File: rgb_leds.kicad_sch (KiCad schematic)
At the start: 28 parts

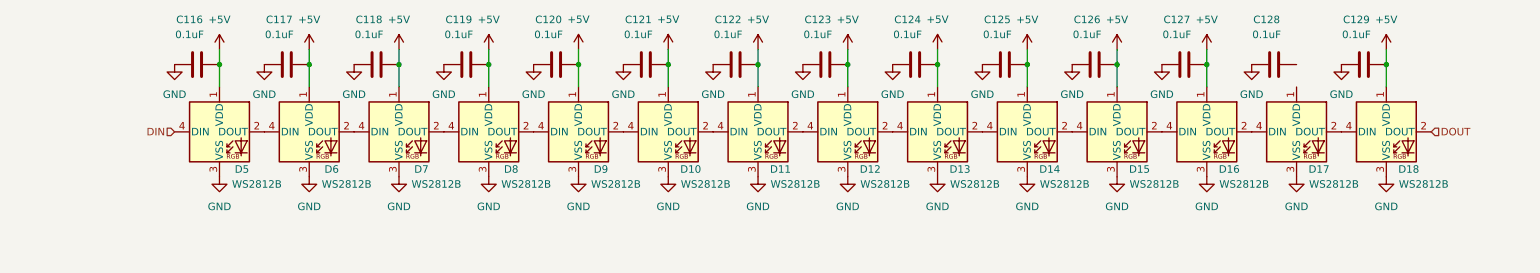
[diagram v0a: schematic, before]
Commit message: usb power source added, need to reassemble to 4-layers
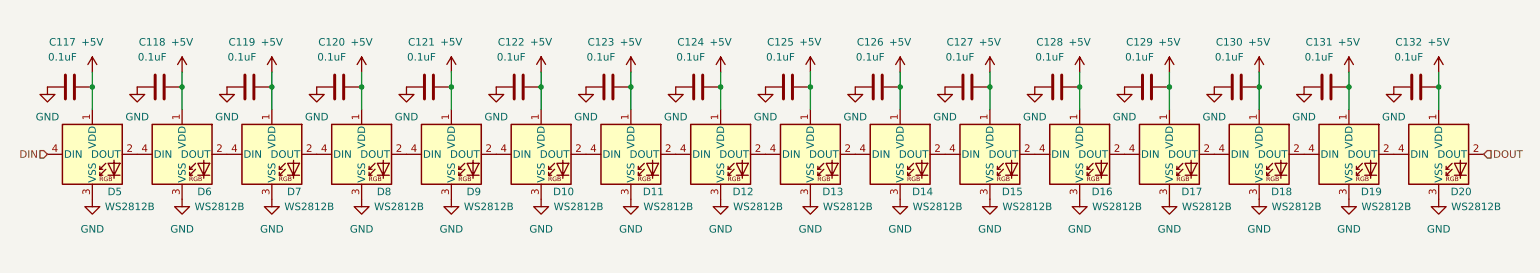
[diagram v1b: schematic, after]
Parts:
- added C129, C130: 0.1uF, Capacitor_SMD:C_0603_1608Metric_Pad1.08x0.95mm_HandSolder, symbol Device:C
- added D17, D18: WS2812B, LED_SMD:LED_WS2812B_PLCC4_5.0x5.0mm_P3.2mm, symbol LED:WS2812B
- renumbered C116 to C117, C117 to C118, C118 to C119, C119 to C120, C120 to C121, C121 to C122, C122 to C123, C123 to C124, C124 to C125, C125 to C126, C126 to C127, C127 to C128, C128 to C131, C129 to C132, D17 to D19, D18 to D20
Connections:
- net +5V: now also C131.2, D19.1 (VDD), C129.2, C130.2, D17.1 (VDD), D18.1 (VDD)
- net GND: now also C129.1, C130.1, D17.3 (VSS), D18.3 (VSS)
- net at D19.4 (DIN): now also D18.2 (DOUT); no longer D16.2 (DOUT)
- new net: D17.2 (DOUT), D18.4 (DIN)
- new net: D16.2 (DOUT), D17.4 (DIN)
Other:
- moved on the sheet: C117, C118, C119, C120, C121, C122, C123, C124, C125, C126, C127, C128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

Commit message: done first iteration of pcb routing, slikscreen still broken
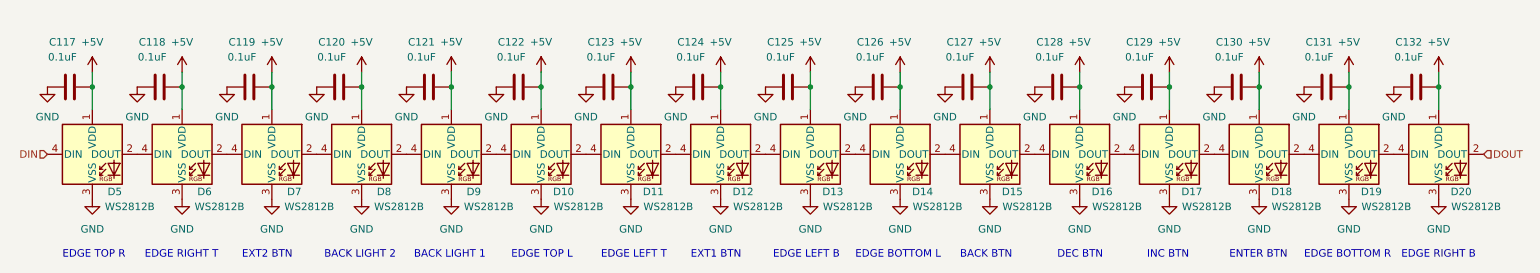
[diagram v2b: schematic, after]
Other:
- note added: "BACK BTN"
- note added: "BACK LIGHT 1"
- note added: "BACK LIGHT 2"
- note added: "DEC BTN"
- note added: "EDGE BOTTOM L"
- note added: "EDGE BOTTOM R"
- note added: "EDGE LEFT B"
- note added: "EDGE LEFT T"
- note added: "EDGE RIGHT B"
- note added: "EDGE RIGHT T"
- note added: "EDGE TOP L"
- note added: "EDGE TOP R"
- note added: "ENTER BTN"
- note added: "EXT1 BTN"
- note added: "EXT2 BTN"
- note added: "INC BTN"

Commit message: mounting holes, fixes silkscreen
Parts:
- renumbered C117 to C115, C118 to C116, C119 to C117, C120 to C118, C121 to C119, C122 to C120, C123 to C121, C124 to C122, C125 to C123, C126 to C124, C127 to C125, C128 to C126, C129 to C127, C130 to C128, C131 to C129, C132 to C130

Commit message: copied own LED footprint, modified silkscreen, minor visual changes in schematics
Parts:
- D10, D11, D12, D13, D14, D15, D16, D17, D18, D19, D20, D5, D6, D7, D8, D9: footprint LED_SMD:LED_WS2812B_PLCC4_5.0x5.0mm_P3.2mm -> airsoft_controller:LED_WS2812B_PLCC4_5.0x5.0mm_P3.2mm
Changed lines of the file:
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@@
     (property "Reference" "D15" (id 0) (at 193.04 97.79 0))
     (property "Value" "WS2812B" (id 1) (at 195.58 100.33 0))
-    (property "Footprint" "LED_SMD:LED_WS2812B_PLCC4_5.0x5.0mm_P3.2mm" (id 2) (at 190.5 99.06 0)
+    (property "Footprint" "airsoft_controller:LED_WS2812B_PLCC4_5.0x5.0mm_P3.2mm" (id 2) (at 190.5 99.06 0)
       (effects (font (size 1.27 1.27)) (justify left top) hide)
     )
@@
     (property "Reference" "D13" (id 0) (at 162.56 97.79 0))
     (property "Value" "WS2812B" (id 1) (at 165.1 100.33 0))
-    (property "Footprint" "LED_SMD:LED_WS2812B_PLCC4_5.0x5.0mm_P3.2mm" (id 2) (at 160.02 99.06 0)
+    (property "Footprint" "airsoft_controller:LED_WS2812B_PLCC4_5.0x5.0mm_P3.2mm" (id 2) (at 160.02 99.06 0)
       (effects (font (size 1.27 1.27)) (justify left top) hide)
     )
@@
     (property "Reference" "D11" (id 0) (at 132.08 97.79 0))
     (property "Value" "WS2812B" (id 1) (at 134.62 100.33 0))
-    (property "Footprint" "LED_SMD:LED_WS2812B_PLCC4_5.0x5.0mm_P3.2mm" (id 2) (at 129.54 99.06 0)
+    (property "Footprint" "airsoft_controller:LED_WS2812B_PLCC4_5.0x5.0mm_P3.2mm" (id 2) (at 129.54 99.06 0)
       (effects (font (size 1.27 1.27)) (justify left top) hide)
     )
@@
     (property "Reference" "D7" (id 0) (at 71.12 97.79 0))
     (property "Value" "WS2812B" (id 1) (at 73.66 100.33 0))
-    (property "Footprint" "LED_SMD:LED_WS2812B_PLCC4_5.0x5.0mm_P3.2mm" (id 2) (at 68.58 99.06 0)
+    (property "Footprint" "airsoft_controller:LED_WS2812B_PLCC4_5.0x5.0mm_P3.2mm" (id 2) (at 68.58 99.06 0)
       (effects (font (size 1.27 1.27)) (justify left top) hide)
     )
@@
     (property "Reference" "D18" (id 0) (at 238.76 97.79 0))
     (property "Value" "WS2812B" (id 1) (at 241.3 100.33 0))
-    (property "Footprint" "LED_SMD:LED_WS2812B_PLCC4_5.0x5.0mm_P3.2mm" (id 2) (at 236.22 99.06 0)
+    (property "Footprint" "airsoft_controller:LED_WS2812B_PLCC4_5.0x5.0mm_P3.2mm" (id 2) (at 236.22 99.06 0)
       (effects (font (size 1.27 1.27)) (justify left top) hide)
     )
@@
     (property "Reference" "D8" (id 0) (at 86.36 97.79 0))
     (property "Value" "WS2812B" (id 1) (at 88.9 100.33 0))
-    (property "Footprint" "LED_SMD:LED_WS2812B_PLCC4_5.0x5.0mm_P3.2mm" (id 2) (at 83.82 99.06 0)
+    (property "Footprint" "airsoft_controller:LED_WS2812B_PLCC4_5.0x5.0mm_P3.2mm" (id 2) (at 83.82 99.06 0)
       (effects (font (size 1.27 1.27)) (justify left top) hide)
     )
@@
     (property "Reference" "D20" (id 0) (at 269.24 97.79 0))
     (property "Value" "WS2812B" (id 1) (at 271.78 100.33 0))
-    (property "Footprint" "LED_SMD:LED_WS2812B_PLCC4_5.0x5.0mm_P3.2mm" (id 2) (at 266.7 99.06 0)
+    (property "Footprint" "airsoft_controller:LED_WS2812B_PLCC4_5.0x5.0mm_P3.2mm" (id 2) (at 266.7 99.06 0)
       (effects (font (size 1.27 1.27)) (justify left top) hide)
     )
@@
     (property "Reference" "D10" (id 0) (at 116.84 97.79 0))
     (property "Value" "WS2812B" (id 1) (at 119.38 100.33 0))
-    (property "Footprint" "LED_SMD:LED_WS2812B_PLCC4_5.0x5.0mm_P3.2mm" (id 2) (at 114.3 99.06 0)
+    (property "Footprint" "airsoft_controller:LED_WS2812B_PLCC4_5.0x5.0mm_P3.2mm" (id 2) (at 114.3 99.06 0)
       (effects (font (size 1.27 1.27)) (justify left top) hide)
     )
@@
     (property "Reference" "D14" (id 0) (at 177.8 97.79 0))
     (property "Value" "WS2812B" (id 1) (at 180.34 100.33 0))
-    (property "Footprint" "LED_SMD:LED_WS2812B_PLCC4_5.0x5.0mm_P3.2mm" (id 2) (at 175.26 99.06 0)
+    (property "Footprint" "airsoft_controller:LED_WS2812B_PLCC4_5.0x5.0mm_P3.2mm" (id 2) (at 175.26 99.06 0)
       (effects (font (size 1.27 1.27)) (justify left top) hide)
     )
@@
     (property "Reference" "D12" (id 0) (at 147.32 97.79 0))
     (property "Value" "WS2812B" (id 1) (at 149.86 100.33 0))
-    (property "Footprint" "LED_SMD:LED_WS2812B_PLCC4_5.0x5.0mm_P3.2mm" (id 2) (at 144.78 99.06 0)
+    (property "Footprint" "airsoft_controller:LED_WS2812B_PLCC4_5.0x5.0mm_P3.2mm" (id 2) (at 144.78 99.06 0)
       (effects (font (size 1.27 1.27)) (justify left top) hide)
     )
@@
     (property "Reference" "D6" (id 0) (at 55.88 97.79 0))
     (property "Value" "WS2812B" (id 1) (at 58.42 100.33 0))
-    (property "Footprint" "LED_SMD:LED_WS2812B_PLCC4_5.0x5.0mm_P3.2mm" (id 2) (at 53.34 99.06 0)
+    (property "Footprint" "airsoft_controller:LED_WS2812B_PLCC4_5.0x5.0mm_P3.2mm" (id 2) (at 53.34 99.06 0)
       (effects (font (size 1.27 1.27)) (justify left top) hide)
     )
@@
     (property "Reference" "D9" (id 0) (at 101.6 97.79 0))
     (property "Value" "WS2812B" (id 1) (at 104.14 100.33 0))
-    (property "Footprint" "LED_SMD:LED_WS2812B_PLCC4_5.0x5.0mm_P3.2mm" (id 2) (at 99.06 99.06 0)
+    (property "Footprint" "airsoft_controller:LED_WS2812B_PLCC4_5.0x5.0mm_P3.2mm" (id 2) (at 99.06 99.06 0)
       (effects (font (size 1.27 1.27)) (justify left top) hide)
     )
@@
     (property "Reference" "D16" (id 0) (at 208.28 97.79 0))
     (property "Value" "WS2812B" (id 1) (at 210.82 100.33 0))
-    (property "Footprint" "LED_SMD:LED_WS2812B_PLCC4_5.0x5.0mm_P3.2mm" (id 2) (at 205.74 99.06 0)
+    (property "Footprint" "airsoft_controller:LED_WS2812B_PLCC4_5.0x5.0mm_P3.2mm" (id 2) (at 205.74 99.06 0)
       (effects (font (size 1.27 1.27)) (justify left top) hide)
     )
@@
     (property "Reference" "D17" (id 0) (at 223.52 97.79 0))
     (property "Value" "WS2812B" (id 1) (at 226.06 100.33 0))
-    (property "Footprint" "LED_SMD:LED_WS2812B_PLCC4_5.0x5.0mm_P3.2mm" (id 2) (at 220.98 99.06 0)
+    (property "Footprint" "airsoft_controller:LED_WS2812B_PLCC4_5.0x5.0mm_P3.2mm" (id 2) (at 220.98 99.06 0)
       (effects (font (size 1.27 1.27)) (justify left top) hide)
     )
@@
     (property "Reference" "D5" (id 0) (at 40.64 97.79 0))
     (property "Value" "WS2812B" (id 1) (at 43.18 100.33 0))
-    (property "Footprint" "LED_SMD:LED_WS2812B_PLCC4_5.0x5.0mm_P3.2mm" (id 2) (at 38.1 99.06 0)
+    (property "Footprint" "airsoft_controller:LED_WS2812B_PLCC4_5.0x5.0mm_P3.2mm" (id 2) (at 38.1 99.06 0)
       (effects (font (size 1.27 1.27)) (justify left top) hide)
     )
@@
     (property "Reference" "D19" (id 0) (at 254 97.79 0))
     (property "Value" "WS2812B" (id 1) (at 256.54 100.33 0))
-    (property "Footprint" "LED_SMD:LED_WS2812B_PLCC4_5.0x5.0mm_P3.2mm" (id 2) (at 251.46 99.06 0)
-      (effects (font (size 1.27 1.27)) (justify left top) hide)
-    )
+    (property "Footprint" "airsoft_controller:LED_WS2812B_PLCC4_5.0x5.0mm_P3.2mm" (id 2) (at 251.46 99.06 0)
+      (effects (font (size 1.27 1.27)) (justify left top) hide)
+    )
